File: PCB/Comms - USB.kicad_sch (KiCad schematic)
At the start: 9 parts, among them J1 USB In, Q1 AO3401A, U1 TPD4E05U06DQAR, U5 LMV321

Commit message: Added large caps to output of TPS2557. Updated STEP file and file data.
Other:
- company: (none) -> Created by Ariamelon (https://github.com/Ariamelon/Honeydew/)
- title: (none) -> Honeydew unified split ergonomic keyboard
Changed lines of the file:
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@@
 (kicad_sch (version 20230121) (generator eeschema)
   (paper "A4")
+  (title_block
+    (title "Honeydew unified split ergonomic keyboard")
+    (date "2023-04-08")
+    (rev "V2.0")
+    (company "Created by Ariamelon (https://github.com/Ariamelon/Honeydew/)")
+    (comment 1 "All capacitors 50V unless otherwise specified.")
+    (comment 2 "Licensed under CC BY 4.0.")
+  )
   (junction (at 105.41 22.86) (diameter 0) (color 0 0 0 0)
   )
@@
   (symbol (lib_id "power:+5V") (at 115.57 27.94 0) (unit 1)
     (in_bom yes) (on_board yes) (dnp no)
-    (property "Reference" "#PWR010" (at 115.57 31.75 0)
+    (property "Reference" "#PWR?" (at 115.57 31.75 0)
       (effects (font (size 1.27 1.27)) hide)
     )
@@
       (project "Honeydew"
         (path "/534caec7-cf60-4f90-b1ed-42c9d445ef0f"
-          (reference "#PWR010") (unit 1)
+          (reference "#PWR?") (unit 1)
         )
         (path "/534caec7-cf60-4f90-b1ed-42c9d445ef0f/0e23afb1-1d24-49d7-b6b4-dea31b732359"
@@
   (symbol (lib_id "power:+5V") (at 105.41 20.32 0) (unit 1)
     (in_bom yes) (on_board yes) (dnp no)
-    (property "Reference" "#PWR010" (at 105.41 24.13 0)
+    (property "Reference" "#PWR?" (at 105.41 24.13 0)
       (effects (font (size 1.27 1.27)) hide)
     )
@@
       (project "Honeydew"
         (path "/534caec7-cf60-4f90-b1ed-42c9d445ef0f"
-          (reference "#PWR010") (unit 1)
+          (reference "#PWR?") (unit 1)
         )
         (path "/534caec7-cf60-4f90-b1ed-42c9d445ef0f/0e23afb1-1d24-49d7-b6b4-dea31b732359"

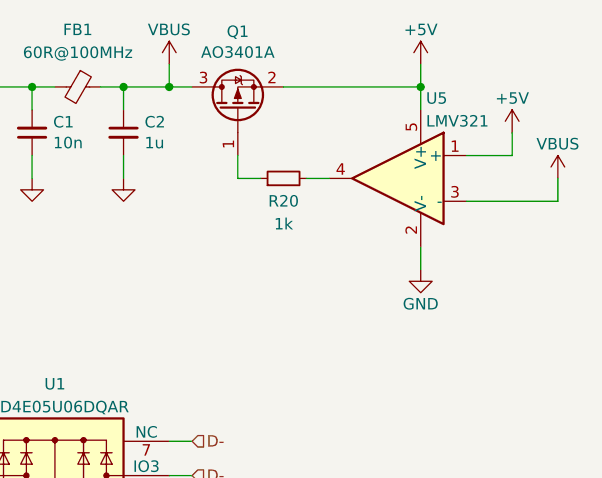
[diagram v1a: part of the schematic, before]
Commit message: Added plate DXF and gerbers. Removed split comms ports and ideal diode.
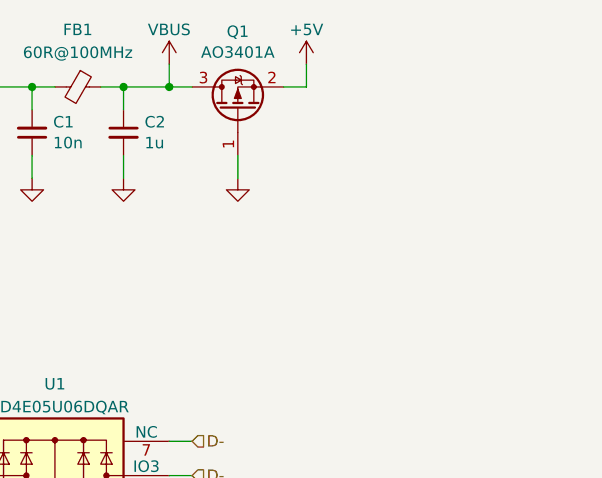
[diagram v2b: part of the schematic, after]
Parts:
- removed R20: 1k, Resistor_SMD:R_0402_1005Metric, symbol Device:R_Small
- removed U5: LMV321, Package_TO_SOT_SMD:SOT-23-5, symbol Amplifier_Operational:LM321
- J1: footprint Honeydew:HRO-TYPE-C-31-M-12 -> Honeydew:HRO-TYPE-C-31-M-13x
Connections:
- net GND: now also Q1.1 (G)
